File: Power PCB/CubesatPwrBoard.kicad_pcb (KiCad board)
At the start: 2 copper layers, 90 x 96 mm, 65 parts, among them J1 Conn_01x04_Female, J10 S1, J11 S2, J12 S3, J13 S4, J14 S5, J15 S6, J2 Conn_01x04_Female, J3 254TR, J4 254TR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

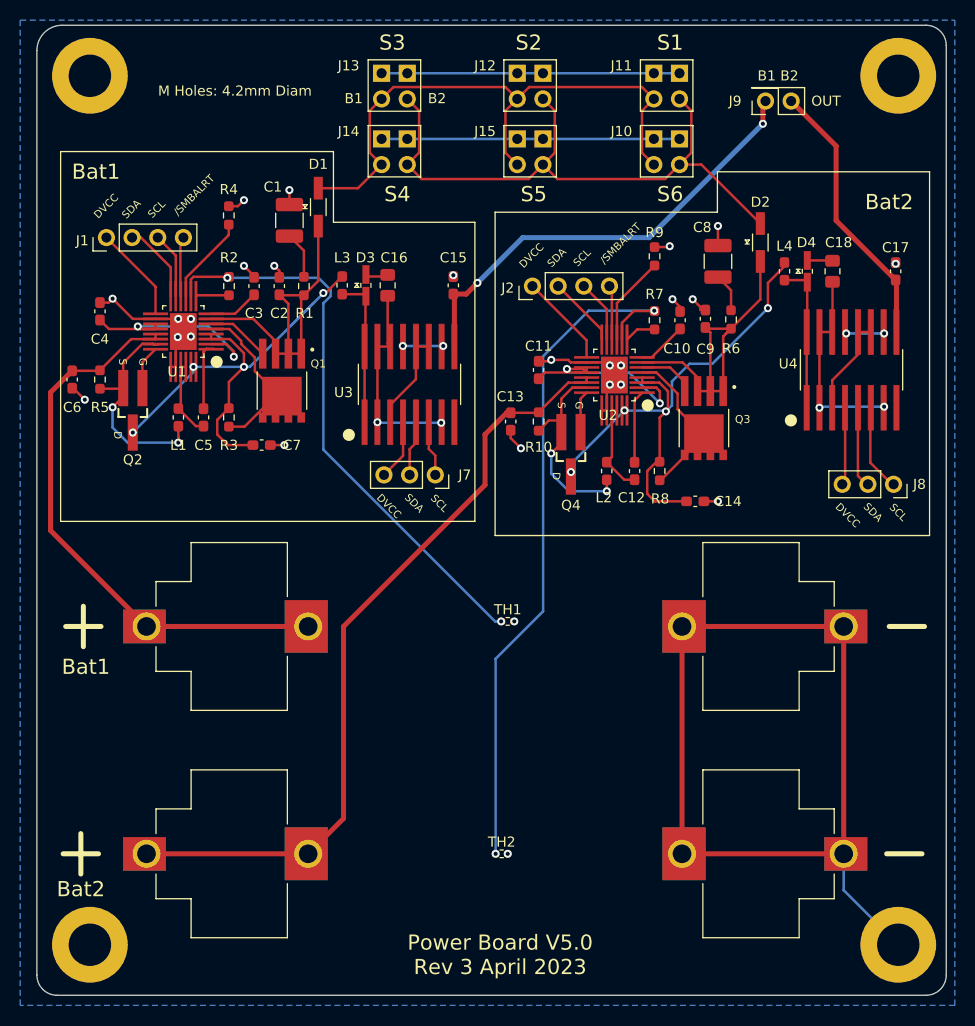
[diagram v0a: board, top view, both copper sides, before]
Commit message: Rotated one text symboland realigned mounting holes
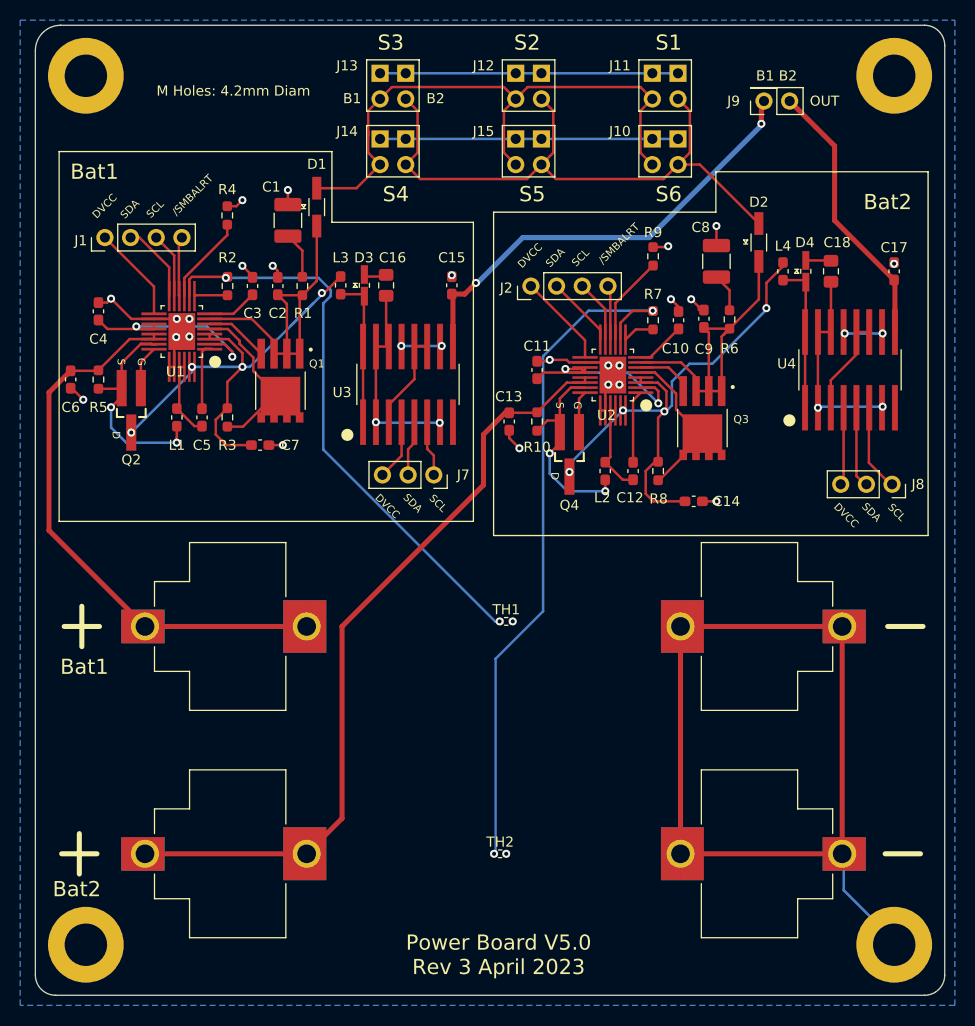
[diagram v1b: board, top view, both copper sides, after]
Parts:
- moved H1 0.40 mm to (111.5, 136.5)
- moved H2 0.40 mm to (191.5, 50.5)
- moved H3 0.40 mm to (191.5, 136.5)
- moved H4 0.40 mm to (111.5, 50.5)
- moved C1 0.15 mm to (131.5, 64.8)
- moved C10 0.15 mm to (170.2, 74.7)
- moved C11 0.15 mm to (156.2, 79.6)
- moved C12 0.15 mm to (165.7, 89.6)
- moved C14 0.15 mm to (171.7, 92.6)
- moved C15 0.15 mm to (147.7, 71.2)
- moved C16 0.15 mm to (141.2, 71.2)
- moved C2 0.15 mm to (130.5, 71.3)
- moved C3 0.15 mm to (128.0, 71.3)
- moved C7 0.15 mm to (128.7, 87.0)
- moved C8 0.15 mm to (173.9, 68.9)
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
